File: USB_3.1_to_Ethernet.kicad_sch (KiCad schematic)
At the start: 43 parts, among them J1 RJ45_JK0654219, U1 LAN7801_9JX, U2 93LC56B_SN, U3 KSZ9031RNXCC, Y1 25MHz, Y2 25MHz

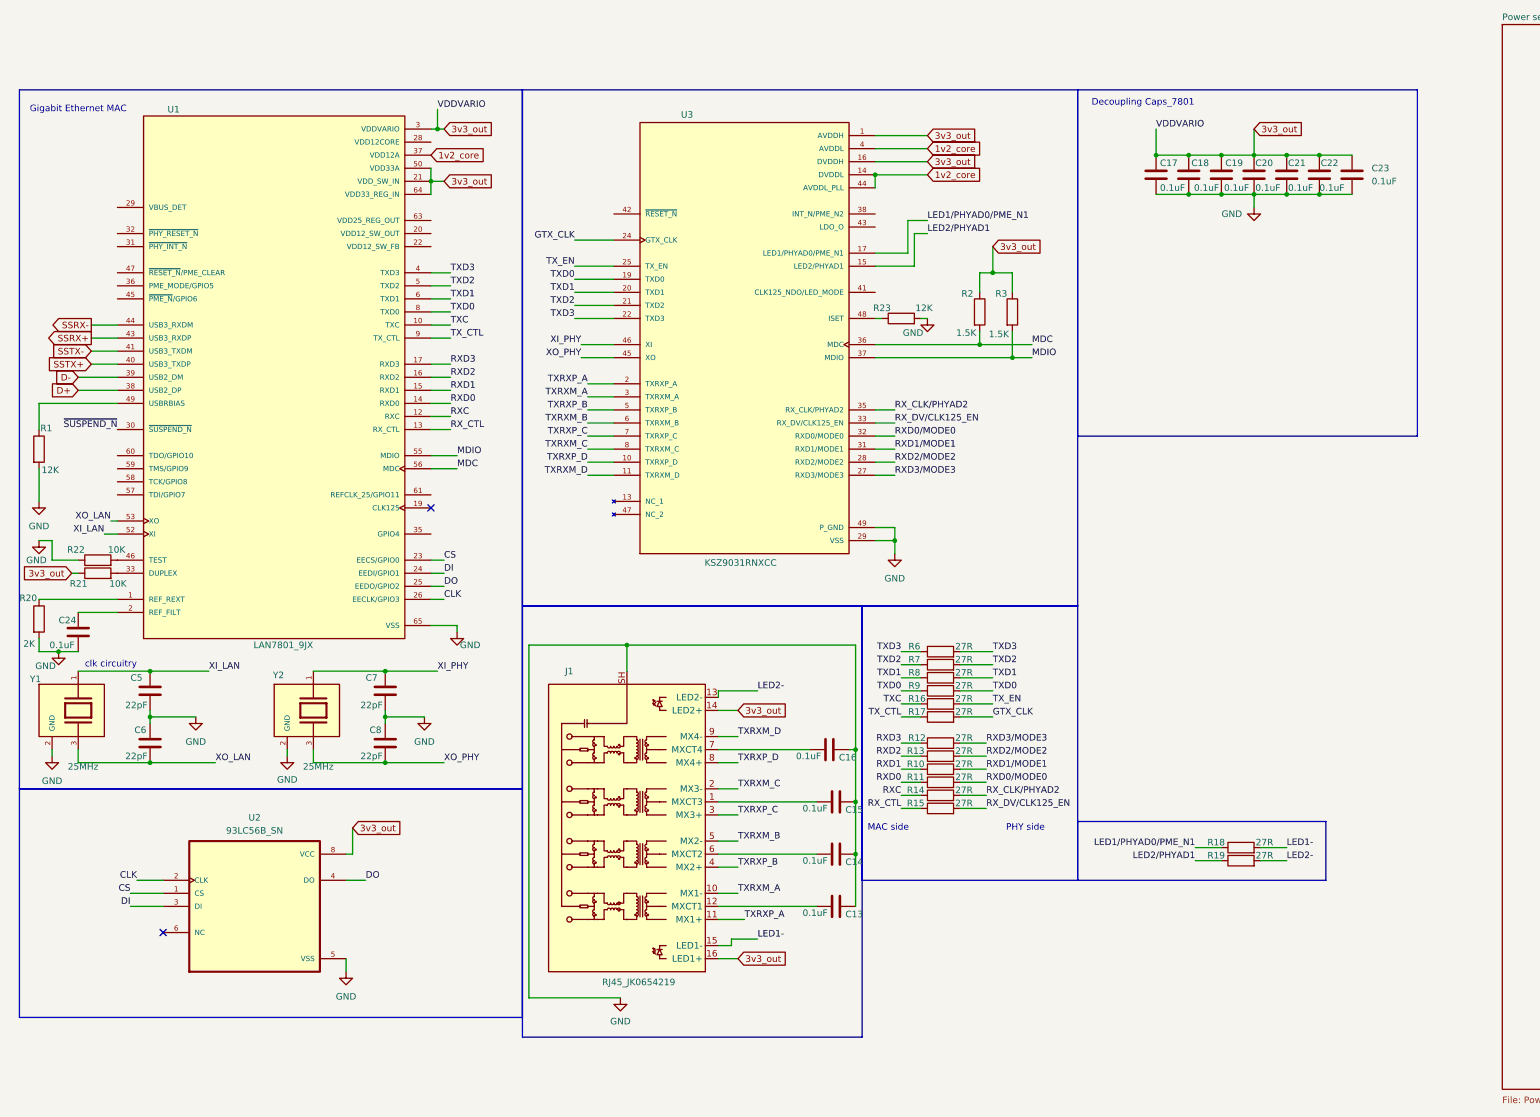
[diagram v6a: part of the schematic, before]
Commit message: 1. Layout placement started. placed Lan7801, PHY, EEPROM and regulators 2.changed D+ D- lines of USB-TVS diode reveresed for clean routing
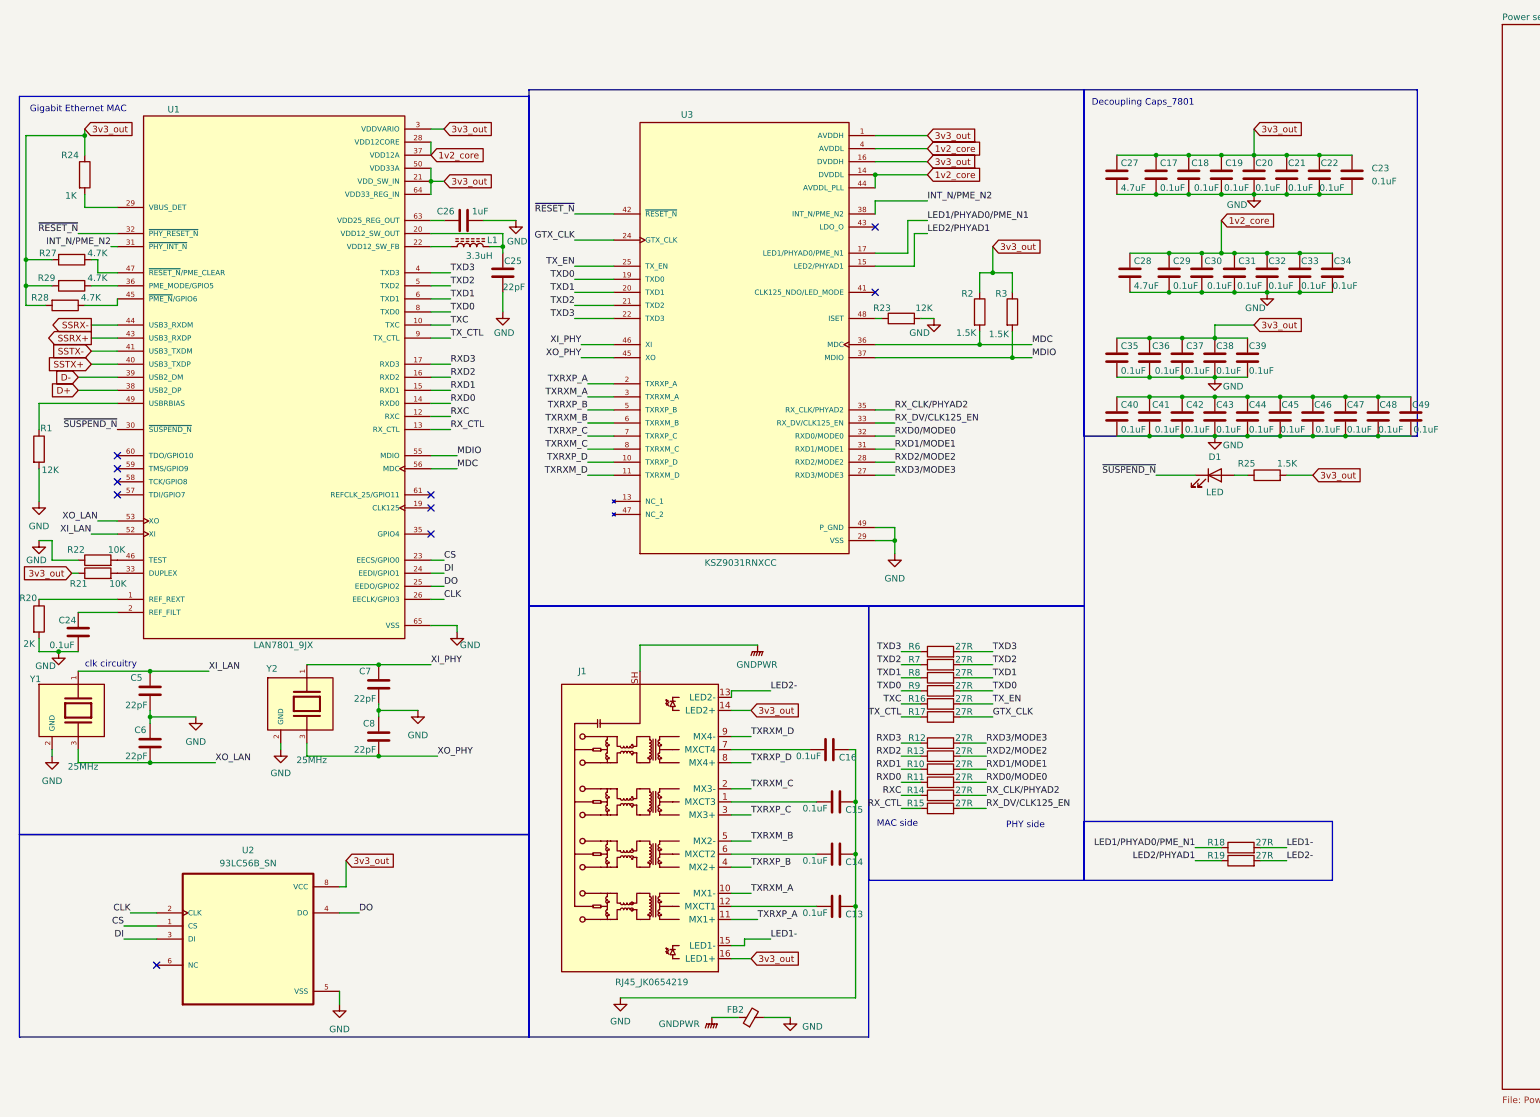
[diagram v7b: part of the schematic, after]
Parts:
- added C25: 22pF, Capacitor_SMD:C_01005_0402Metric, symbol Device:C
- added C26: 1uF, Capacitor_SMD:C_01005_0402Metric, symbol Device:C
- added C27, C28: 4.7uF, Capacitor_SMD:C_01005_0402Metric, symbol Device:C
- added C29, C30, C31, C32, C33, C34, C35, C36, C37, C38, C39, C40, C41, C42, C43, C44, C45, C46, C47, C48, C49: 0.1uF, Capacitor_SMD:C_01005_0402Metric, symbol Device:C
- added D1: LED, LED_SMD:LED_01005_0402Metric, symbol Device:LED
- added FB2: FerriteBead_Small, Inductor_SMD:L_0402_1005Metric, symbol Device:FerriteBead_Small
- added L1: 3.3uH, Inductor_SMD:L_0402_1005Metric, symbol Device:L_Ferrite
- added R24: 1K, Resistor_SMD:R_0402_1005Metric, symbol Device:R
- added R25: 1.5K, Resistor_SMD:R_0402_1005Metric, symbol Device:R
- added R27, R28, R29: 4.7K, Resistor_SMD:R_0402_1005Metric, symbol Device:R
- C13, C14, C15, C16: footprint Capacitor_SMD:C_1206_3216Metric_Pad1.33x1.80mm_HandSolder -> Capacitor_SMD:C_0402_1005Metric
- C5, C6, C7, C8: footprint Capacitor_SMD:C_0603_1608Metric -> Capacitor_SMD:C_0402_1005Metric
- R1, R20, R21, R22, R23: footprint Capacitor_SMD:C_01005_0402Metric -> Resistor_SMD:R_0402_1005Metric
- R10, R11, R12, R13, R14, R15, R16, R17, R18, R19, R6, R7, R8, R9: footprint Resistor_SMD:R_1206 -> Resistor_SMD:R_0402_1005Metric
- R2, R3: footprint Resistor_SMD:R_1206_3216Metric -> Resistor_SMD:R_0402_1005Metric
- Y1, Y2: footprint Crystal:XTAL_ABMM325000MHZET -> Crystal:Crystal_SMD_3225-4Pin_3.2x2.5mm
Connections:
- net VDD12CORE is gone; now on net AVDDL: U1.28 (VDD12CORE), U1.54 (VDD12CORE)
- net AVDDH: now also C27.1, C35.1, C36.1, C37.1, C38.1, C39.1, R24.1, R25.2, R27.2, R28.2, R29.2
- net AVDDL: now also C28.1, C29.1, C30.1, C31.1, C32.1, C33.1, C34.1
- net GND: now also C25.2, C26.2, C27.2, C28.2, C29.2, C30.2, C31.2, C32.2, C33.2, C34.2, C35.2, C36.2, C37.2, C38.2, C39.2, C40.2, C41.2, C42.2, C43.2, C44.2, C45.2, C46.2, C47.2, C48.2, C49.2, FB2.2; no longer J1.SH
- net ~{SUSPEND_N}: now also D1.1 (K)
- net INT_N/PME_N2: now reaches U3.38 (INT_N/PME_N2)
- net INT_N/PME_N2: now also U1.31 (~{PHY_INT_N})
- net ~{RESET_N}: now reaches U3.42 (~{RESET_N})
- net ~{RESET_N}: now also U1.32 (~{PHY_RESET_N})
- net at U1.20 (VDD12_SW_OUT): now also C25.1, L1.2
- net at U1.22 (VDD12_SW_FB): now also L1.1
- net at U1.29 (VBUS_DET): now also R24.2
- net at U1.36 (PME_MODE/GPIO5): now also R29.1
- net at U1.45 (~{PME_N}/GPIO6): now also R28.1
- net at U1.47 (~{RESET_N}/PME_CLEAR): now also R27.1
- net at U1.63 (VDD25_REG_OUT): now also C26.1
- new net: C40.1, C41.1, C42.1, C43.1, C44.1, C45.1, C46.1, C47.1, C48.1, C49.1
- new net: D1.2 (A), R25.1
- new net GNDPWR: FB2.1, J1.SH
- no-connect marks 2 -> 10
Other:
- moved on the sheet: C7, C8, J1, U2, Y2

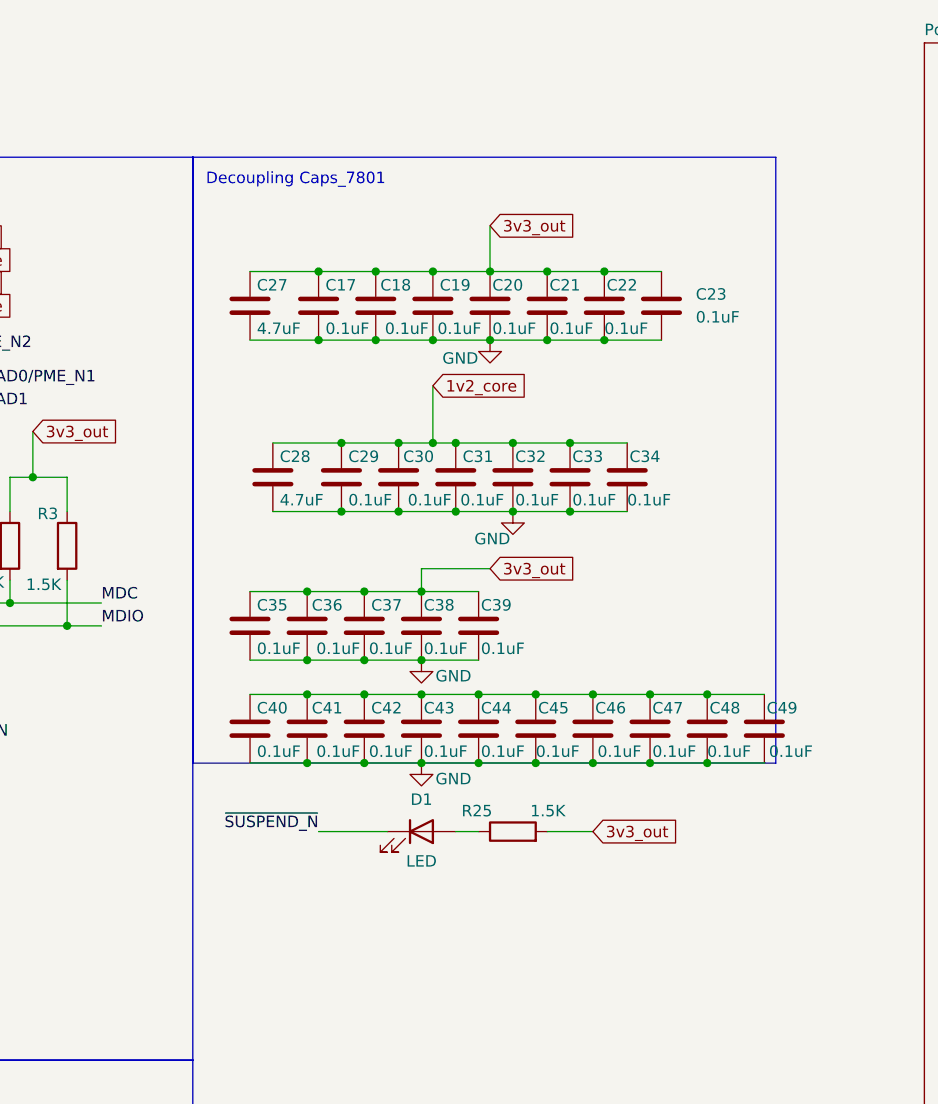
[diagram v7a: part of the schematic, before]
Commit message: 1. Major routing done- usb3.1,usb2, >> 2. buck converter and voltage regulators placement and routing done >> 3. Decoupling caps added
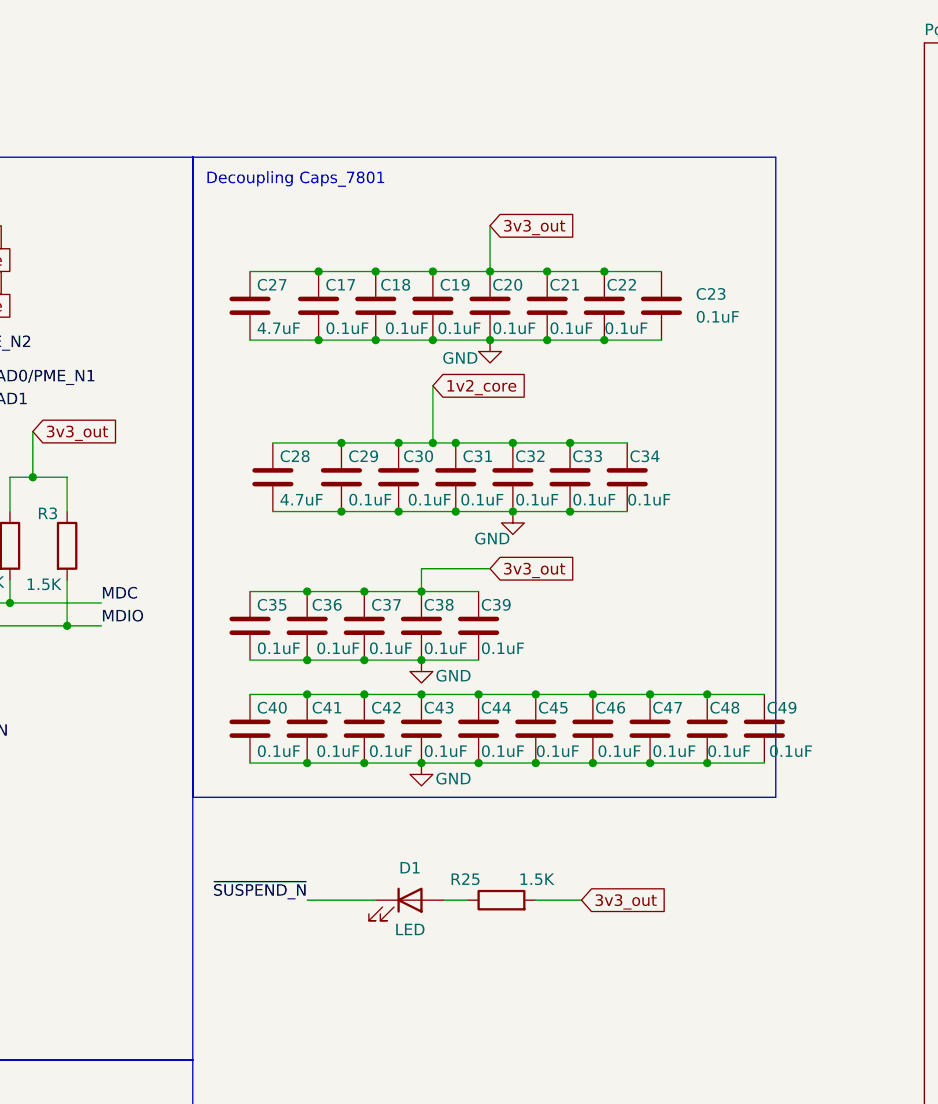
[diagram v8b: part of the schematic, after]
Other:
- moved on the sheet: D1, R25
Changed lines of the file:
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@@
 	(rectangle
 		(start 219.71 12.7)
-		(end 284.48 80.01)
+		(end 284.48 83.82)
 		(stroke
 			(width 0)
@@
 	(wire
 		(pts
-			(xy 264.16 87.63) (xy 259.08 87.63)
+			(xy 262.89 95.25) (xy 257.81 95.25)
 		)
 		(stroke
@@
 	(wire
 		(pts
-			(xy 233.68 87.63) (xy 241.3 87.63)
+			(xy 232.41 95.25) (xy 240.03 95.25)
 		)
 		(stroke
@@
 	(wire
 		(pts
-			(xy 248.92 87.63) (xy 251.46 87.63)
+			(xy 247.65 95.25) (xy 250.19 95.25)
 		)
 		(stroke
@@
 	)
 	(label "~{SUSPEND_N}"
-		(at 233.68 87.63 180)
+		(at 232.41 95.25 180)
 		(effects
 			(font
@@
 	(global_label "3v3_out"
 		(shape input)
-		(at 264.16 87.63 0)
+		(at 262.89 95.25 0)
 		(fields_autoplaced yes)
 		(effects
@@
 		)
 		(property "Intersheetrefs" "${INTERSHEET_REFS}"
-			(at 274.5231 87.63 0)
+			(at 273.2531 95.25 0)
 			(show_name no)
 			(do_not_autoplace no)
@@
 	(symbol
 		(lib_id "Device:R")
-		(at 255.27 87.63 90)
+		(at 254 95.25 90)
 		(unit 1)
 		(body_style 1)
@@
 		(dnp no)
 		(property "Reference" "R25"
-			(at 252.984 85.344 90)
+			(at 251.714 92.964 90)
 			(show_name no)
 			(do_not_autoplace no)
@@
 		)
 		(property "Value" "1.5K"
-			(at 261.112 85.344 90)
+			(at 259.842 92.964 90)
 			(show_name no)
 			(do_not_autoplace no)
@@
 		)
 		(property "Footprint" "Resistor_SMD:R_0402_1005Metric"
-			(at 255.27 89.408 90)
+			(at 254 97.028 90)
 			(hide yes)
 			(show_name no)
@@
 		)
 		(property "Datasheet" ""
-			(at 255.27 87.63 0)
+			(at 254 95.25 0)
 			(hide yes)
 			(show_name no)
@@
 		)
 		(property "Description" "Resistor"
-			(at 255.27 87.63 0)
+			(at 254 95.25 0)
 			(hide yes)
 			(show_name no)
@@
 	(symbol
 		(lib_id "Device:LED")
-		(at 245.11 87.63 0)
+		(at 243.84 95.25 0)
 		(unit 1)
 		(body_style 1)
@@
 		(dnp no)
 		(property "Reference" "D1"
-			(at 245.11 84.074 0)
+			(at 243.84 91.694 0)
 			(show_name no)
 			(do_not_autoplace no)
@@
 		)
 		(property "Value" "LED"
-			(at 245.11 90.932 0)
+			(at 243.84 98.552 0)
 			(show_name no)
 			(do_not_autoplace no)
@@
 		)
 		(property "Footprint" "LED_SMD:LED_01005_0402Metric"
-			(at 245.11 87.63 0)
+			(at 243.84 95.25 0)
 			(hide yes)
 			(show_name no)
@@
 		)
 		(property "Datasheet" ""
-			(at 245.11 87.63 0)
+			(at 243.84 95.25 0)
 			(hide yes)
 			(show_name no)
@@
 		)
 		(property "Description" "Light emitting diode"
-			(at 245.11 87.63 0)
+			(at 243.84 95.25 0)
 			(hide yes)
 			(show_name no)
@@
 		)
 		(property "Sim.Pins" "1=K 2=A"
-			(at 245.11 87.63 0)
+			(at 243.84 95.25 0)
 			(hide yes)
 			(show_name no)
